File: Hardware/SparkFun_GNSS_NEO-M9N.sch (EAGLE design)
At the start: 54 parts, among them J1 MICROMOD_STANDARD, U1 U-BLOX_NEO-M9N, U2 3.3V, U3 EEPROM, U4 74HC1G04

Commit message: Adds WP pullup resistor and jumper to allow user control over the pin
* Routes WP net to card's edge
* Adds silk to WP jumper
* Adjusts a few traces
* Rolls version to v11
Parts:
- J4: value (none) -> Bus Selection
- renumbered JP1 to WP
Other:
- note added: "Close Jumper to disable Write Protect."
- note added: "The default is I2C and Serial."
- note added: "To use SPI simply move the 2-pin jumper to the side labeled "SPI"."
- note added: "Voltage Regulation: AP2112K"
- note added: "v11"
- note removed: "Default is I2C and Serial"
- note removed: "To use SPI simply move the shunt to the side labeled "SPI"."
- note removed: "Voltage Regulation"
- note removed: "v10"
- moved on the sheet: B1, C1, C2, C3, C4, C5, C6, C7, D1, D2, D3, E1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

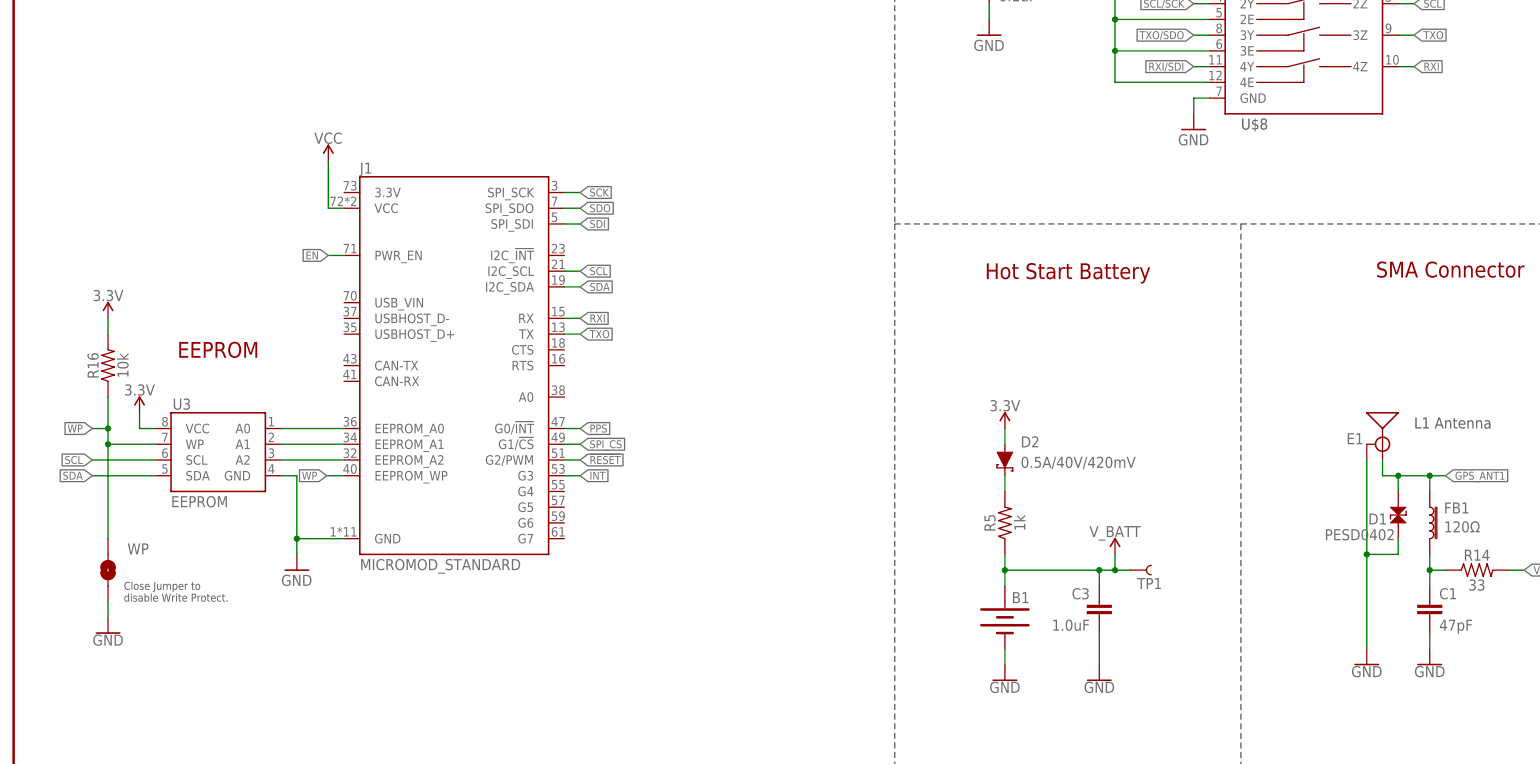
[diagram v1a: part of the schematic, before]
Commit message: Add 0.1uF bypass cap to EEPROM VCC, moves two PTH header east to accommodate new cap
* Adds "GNSS" silk
* Flips silk on bottom so that all silk has uniform direction
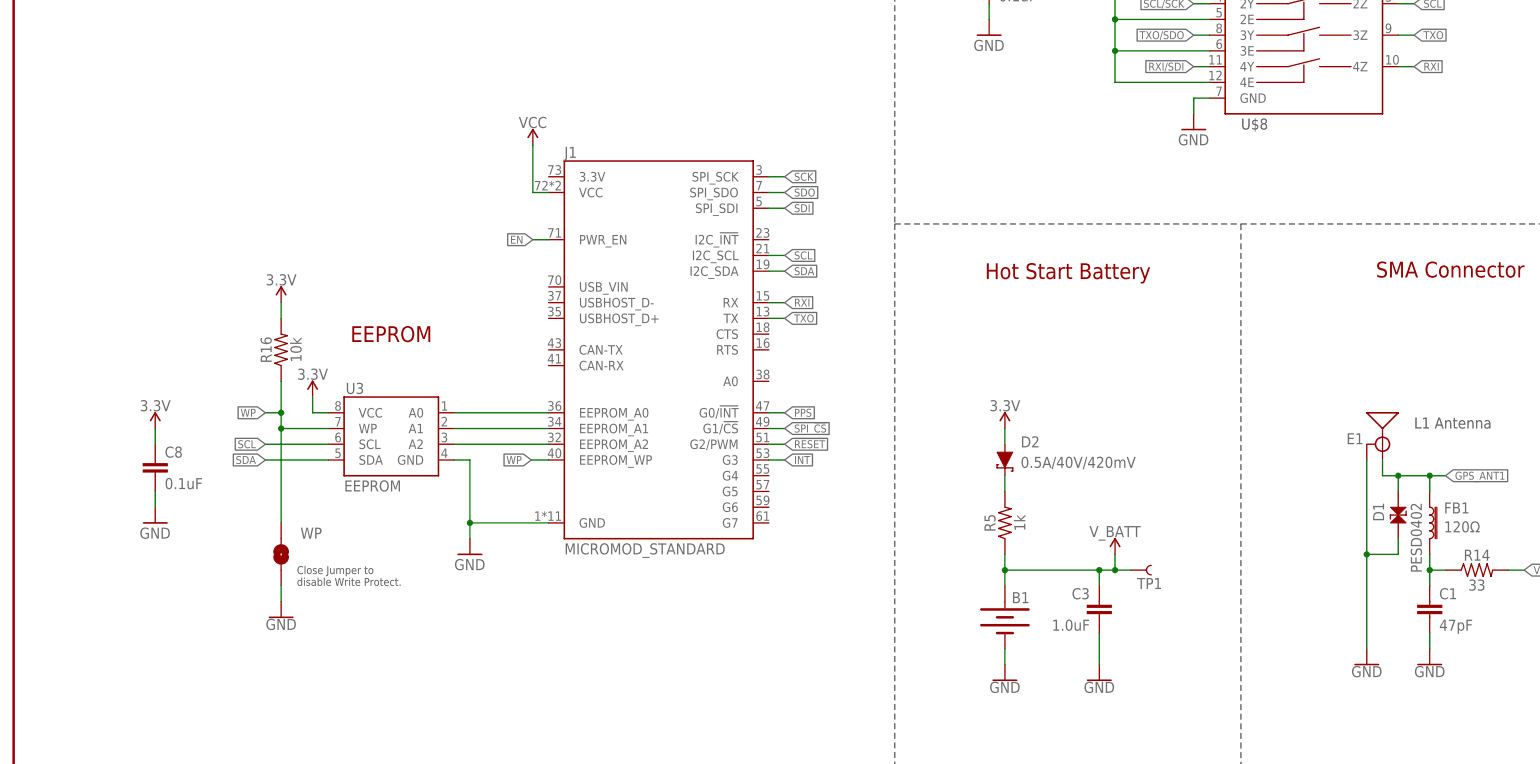
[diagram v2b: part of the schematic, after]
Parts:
- added C8: 0.1uF, SparkFun-Capacitors:0.1UF-0603-25V-(+80/-20%)
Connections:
- net 3.3V: now also C8.1
- net GND: now also C8.2
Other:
- moved on the sheet: J1, R16, U3, WP

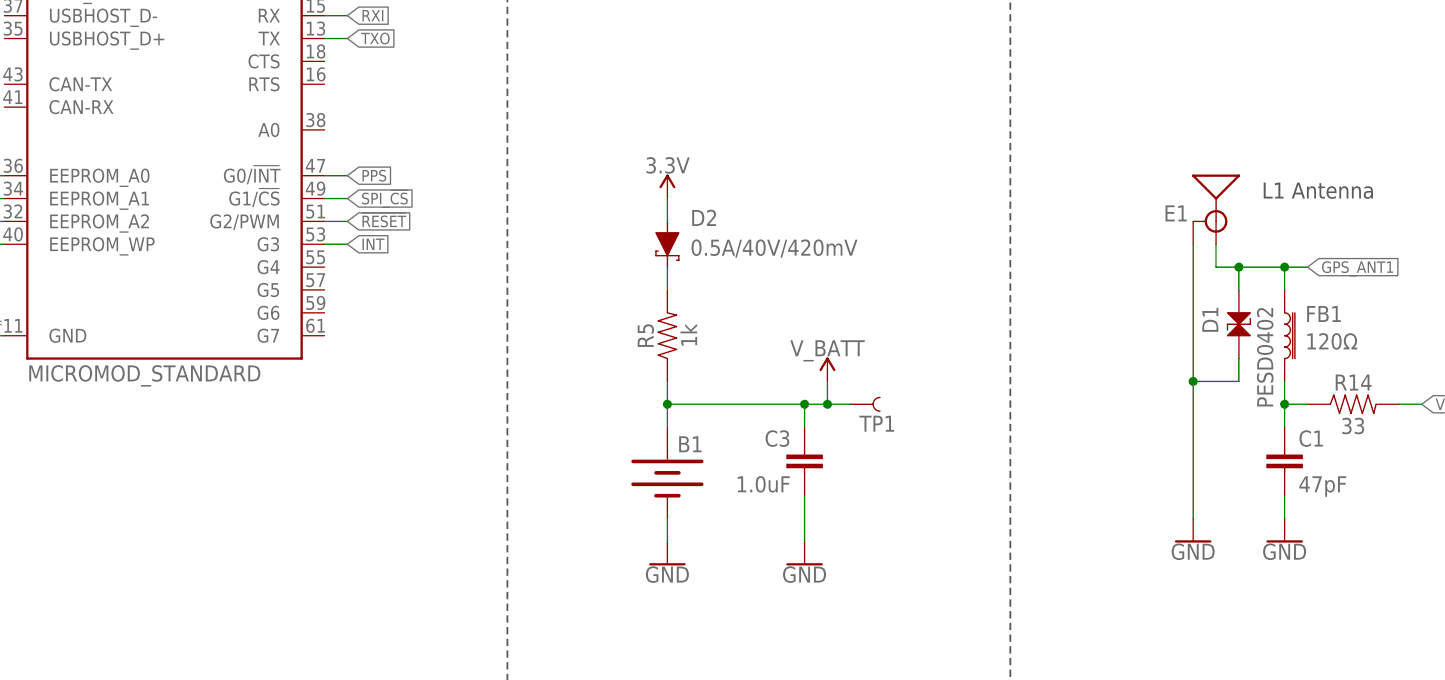
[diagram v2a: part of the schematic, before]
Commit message: Updates Function Board symbol
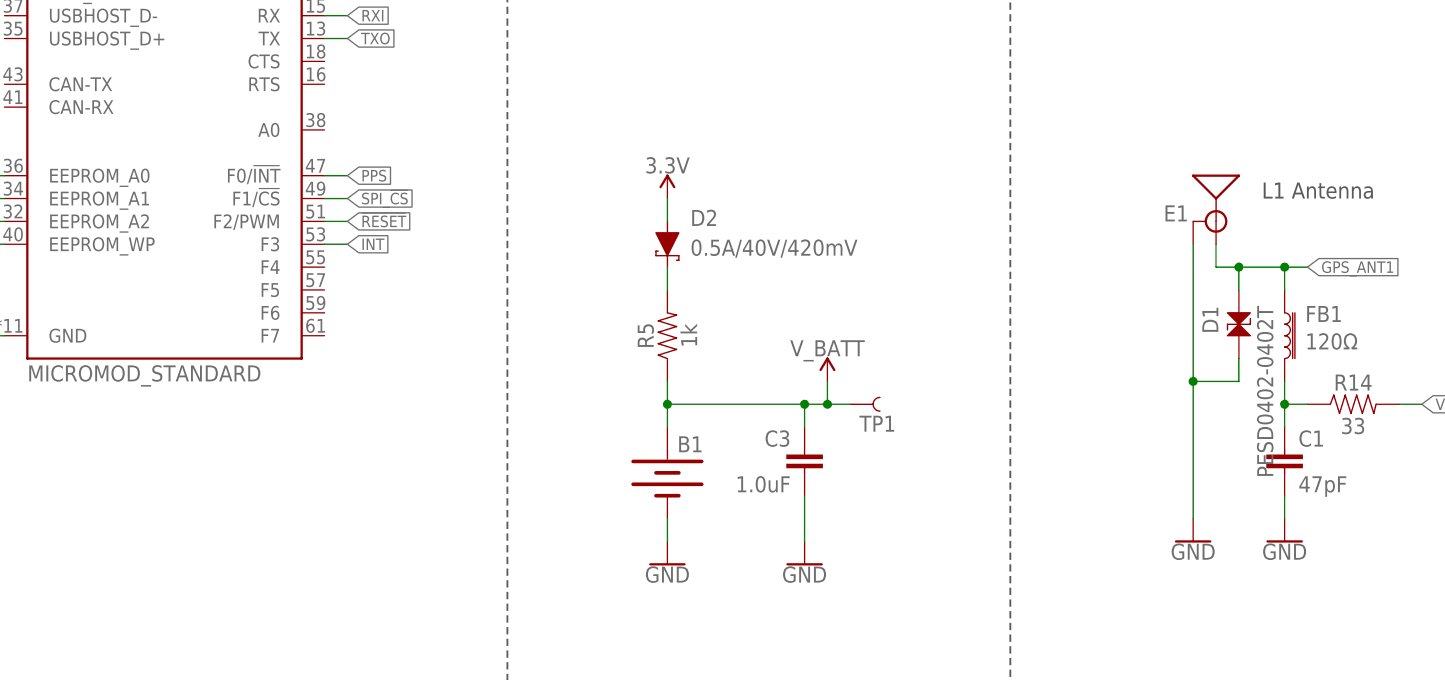
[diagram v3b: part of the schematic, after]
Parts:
- D1: value PESD0402 -> PESD0402-0402T; device SparkFun-DiscreteSemi:PESD0402 -> SparkFun-DiscreteSemi:PESD0402-0402T
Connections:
- net !RESET: now also J1.F2/PWM; no longer J1.G2/PWM
- net INT: now also J1.F3; no longer J1.G3
- net PPS: now also J1.F0/!INT!; no longer J1.G0/!INT!
- net SPI_!CS!: now also J1.F1/!CS!; no longer J1.G1/!CS!
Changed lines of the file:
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@@
 <part name="SUPPLY10" library="SparkFun-PowerSymbols" deviceset="3.3V" device=""/>
 <part name="GND9" library="SparkFun-PowerSymbols" deviceset="GND" device=""/>
-<part name="D1" library="SparkFun-DiscreteSemi" deviceset="PESD0402" device=""/>
+<part name="D1" library="SparkFun-DiscreteSemi" deviceset="PESD0402" device="-0402T"/>
 <part name="J2" library="SparkFun-Connectors" deviceset="CONN_02" device=""/>
 <part name="LOGO2" library="SparkFun-Aesthetics" deviceset="SFE_LOGO_NAME_FLAME" device=".2_INCH" value="SFE_LOGO_NAME_FLAME.2_INCH"/>
@@
 <attribute name="VALUE" x="43.18" y="30.226" size="1.778" layer="96" align="top-center"/>
 </instance>
-<instance part="D1" gate="G$1" x="223.52" y="45.72" smashed="yes" rot="R90">
+<instance part="D1" gate="D1" x="223.52" y="45.72" smashed="yes" rot="R90">
 <attribute name="NAME" x="219.456" y="49.022" size="1.778" layer="95" font="vector" rot="R270"/>
 <attribute name="VALUE" x="227.33" y="49.022" size="1.778" layer="96" font="vector" rot="R270" align="top-left"/>
@@
 <pinref part="E1" gate="G$1" pin="GND"/>
 <wire x1="218.44" y1="55.88" x2="218.44" y2="40.64" width="0.1524" layer="91"/>
-<pinref part="D1" gate="G$1" pin="1"/>
+<pinref part="D1" gate="D1" pin="1"/>
 <wire x1="218.44" y1="40.64" x2="218.44" y2="25.4" width="0.1524" layer="91"/>
 <wire x1="223.52" y1="43.18" x2="223.52" y2="40.64" width="0.1524" layer="91"/>
@@
 <wire x1="121.92" y1="58.42" x2="124.46" y2="58.42" width="0.1524" layer="91"/>
 <label x="124.46" y="58.42" size="1.27" layer="95" font="vector" xref="yes"/>
-<pinref part="J1" gate="J1" pin="G2/PWM"/>
+<pinref part="J1" gate="J1" pin="F2/PWM"/>
 </segment>
 </net>
@@
 </segment>
 <segment>
-<pinref part="J1" gate="J1" pin="G3"/>
+<pinref part="J1" gate="J1" pin="F3"/>
 <wire x1="121.92" y1="55.88" x2="124.46" y2="55.88" width="0.1524" layer="91"/>
 <label x="124.46" y="55.88" size="1.27" layer="95" xref="yes"/>
@@
 <wire x1="121.92" y1="63.5" x2="124.46" y2="63.5" width="0.1524" layer="91"/>
 <label x="124.46" y="63.5" size="1.27" layer="95" font="vector" xref="yes"/>
-<pinref part="J1" gate="J1" pin="G0/!INT!"/>
+<pinref part="J1" gate="J1" pin="F0/!INT!"/>
 </segment>
 </net>
@@
 <wire x1="228.6" y1="50.8" x2="228.6" y2="53.34" width="0.1524" layer="91"/>
 <junction x="228.6" y="53.34"/>
-<pinref part="D1" gate="G$1" pin="2"/>
+<pinref part="D1" gate="D1" pin="2"/>
 <wire x1="223.52" y1="50.8" x2="223.52" y2="53.34" width="0.1524" layer="91"/>
 <junction x="223.52" y="53.34"/>
@@
 <wire x1="121.92" y1="60.96" x2="124.46" y2="60.96" width="0.1524" layer="91"/>
 <label x="124.46" y="60.96" size="1.27" layer="95" font="vector" xref="yes"/>
-<pinref part="J1" gate="J1" pin="G1/!CS!"/>
-</segment>
-</net>
+<pinref part="J1" gate="J1" pin="F1/!CS!"/>
+</segment>
+</net>

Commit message: Switches SMA connector to PTH connector
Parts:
- E1: value ANTENNA-SMA-GROUNDEDEDGE_SMA_SMD -> ANTENNA-SMA-GROUNDEDEDGE_SMA; device SparkFun-RF:ANTENNA-SMA-GROUNDEDEDGE_SMA_SMD -> SparkFun-RF:ANTENNA-SMA-GROUNDEDEDGE_SMA
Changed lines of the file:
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@@
 <part name="GND17" library="SparkFun-PowerSymbols" deviceset="GND" device=""/>
 <part name="SUPPLY12" library="SparkFun-PowerSymbols" deviceset="3.3V" device=""/>
-<part name="E1" library="SparkFun-RF" deviceset="ANTENNA-SMA-GROUNDED" device="EDGE_SMA_SMD" value="ANTENNA-SMA-GROUNDEDEDGE_SMA_SMD"/>
+<part name="E1" library="SparkFun-RF" deviceset="ANTENNA-SMA-GROUNDED" device="EDGE_SMA" value="ANTENNA-SMA-GROUNDEDEDGE_SMA"/>
 <part name="FB1" library="SparkFun-Coils" deviceset="FERRITE_BEAD-120_OHM" device="-0402" value="120Ω"/>
 <part name="C1" library="SparkFun-Capacitors" deviceset="47PF" device="-0402-25V-5%-X7R" value="47pF"/>

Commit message: Adds PTH SMA Connector to design
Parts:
- E1: value ANTENNA-SMA-GROUNDEDEDGE_SMA -> ANTENNA-SMA-GROUNDEDEDGE_SMA_THIN; device SparkFun-RF:ANTENNA-SMA-GROUNDEDEDGE_SMA -> SparkFun-RF:ANTENNA-SMA-GROUNDEDEDGE_SMA_THIN
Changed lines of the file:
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@@
 <part name="GND17" library="SparkFun-PowerSymbols" deviceset="GND" device=""/>
 <part name="SUPPLY12" library="SparkFun-PowerSymbols" deviceset="3.3V" device=""/>
-<part name="E1" library="SparkFun-RF" deviceset="ANTENNA-SMA-GROUNDED" device="EDGE_SMA" value="ANTENNA-SMA-GROUNDEDEDGE_SMA"/>
+<part name="E1" library="SparkFun-RF" deviceset="ANTENNA-SMA-GROUNDED" device="EDGE_SMA_THIN" value="ANTENNA-SMA-GROUNDEDEDGE_SMA_THIN"/>
 <part name="FB1" library="SparkFun-Coils" deviceset="FERRITE_BEAD-120_OHM" device="-0402" value="120Ω"/>
 <part name="C1" library="SparkFun-Capacitors" deviceset="47PF" device="-0402-25V-5%-X7R" value="47pF"/>

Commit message: Adds PTH selection silk to bottom
* Chnages MISO/MOSI net label -> PICO/POCI
* Adds text explanation to safeboot pth selection
* Moves some nets around for better ground pour
* Adds a few vias
* Adds measures to LEDs
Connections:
- net RXI/SDI renamed RXI/PICO
- net SDI renamed PICO
- net SDO renamed POCI
- net TXO/SDO renamed TXO/POCI
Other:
- note added: "You can reset your module to factory settings by setting safeboot low while powering up the module."
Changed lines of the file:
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@@
 <text x="45.72" y="35.56" size="1.27" layer="97" font="vector">Close Jumper to
 disable Write Protect.</text>
+<text x="111.76" y="182.118" size="1.27" layer="97" font="vector">You can reset your
+module to factory settings
+by setting safeboot low
+while powering up the
+module.</text>
 </plain>
 <instances>
@@
 </instance>
 <instance part="B1" gate="G$1" x="160.02" y="30.48" smashed="yes" rot="R270">
-<attribute name="NAME" x="162.56" y="32.766" size="1.778" layer="95" font="vector" rot="MR0" align="bottom-center"/>
+<attribute name="NAME" x="163.068" y="33.274" size="1.778" layer="95" font="vector" align="bottom-center"/>
 </instance>
 <instance part="GND5" gate="1" x="160.02" y="20.32" smashed="yes">
@@
 <instance part="D1" gate="D1" x="223.52" y="45.72" smashed="yes" rot="R90">
 <attribute name="NAME" x="219.456" y="49.022" size="1.778" layer="95" font="vector" rot="R270"/>
-<attribute name="VALUE" x="227.33" y="49.022" size="1.778" layer="96" font="vector" rot="R270" align="top-left"/>
 </instance>
 <instance part="J2" gate="G$1" x="96.52" y="193.04" smashed="yes">
@@
 </segment>
 </net>
-<net name="RXI/SDI" class="0">
+<net name="RXI/PICO" class="0">
 <segment>
 <wire x1="104.14" y1="220.98" x2="106.68" y2="220.98" width="0.1524" layer="91"/>
@@
 </segment>
 </net>
-<net name="TXO/SDO" class="0">
+<net name="TXO/POCI" class="0">
 <segment>
 <wire x1="104.14" y1="223.52" x2="106.68" y2="223.52" width="0.1524" layer="91"/>
@@
 </segment>
 </net>
-<net name="SDO" class="0">
+<net name="POCI" class="0">
 <segment>
 <pinref part="U$15" gate="G$1" pin="3Z"/>
@@
 </segment>
 </net>
-<net name="SDI" class="0">
+<net name="PICO" class="0">
 <segment>
 <pinref part="U$15" gate="G$1" pin="4Z"/>
